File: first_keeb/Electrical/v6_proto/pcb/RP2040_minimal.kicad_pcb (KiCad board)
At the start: 2 copper layers, 77.7 x 77.5 mm, 71 parts, among them P1 USB-TYPE-C-016, Q1 SN74LV1T34DBV, SW1 SKRKAGE020, SW2 PTS647 SN70 SMTR2 LFS, SW3 PTS647 SN70 SMTR2 LFS, U1 NCP1117-3.3_SOT223, U2 LM4040DBZ-3, U3 PRTR5V0U2X, U4 W25Q32JVSS, U5 RP2040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

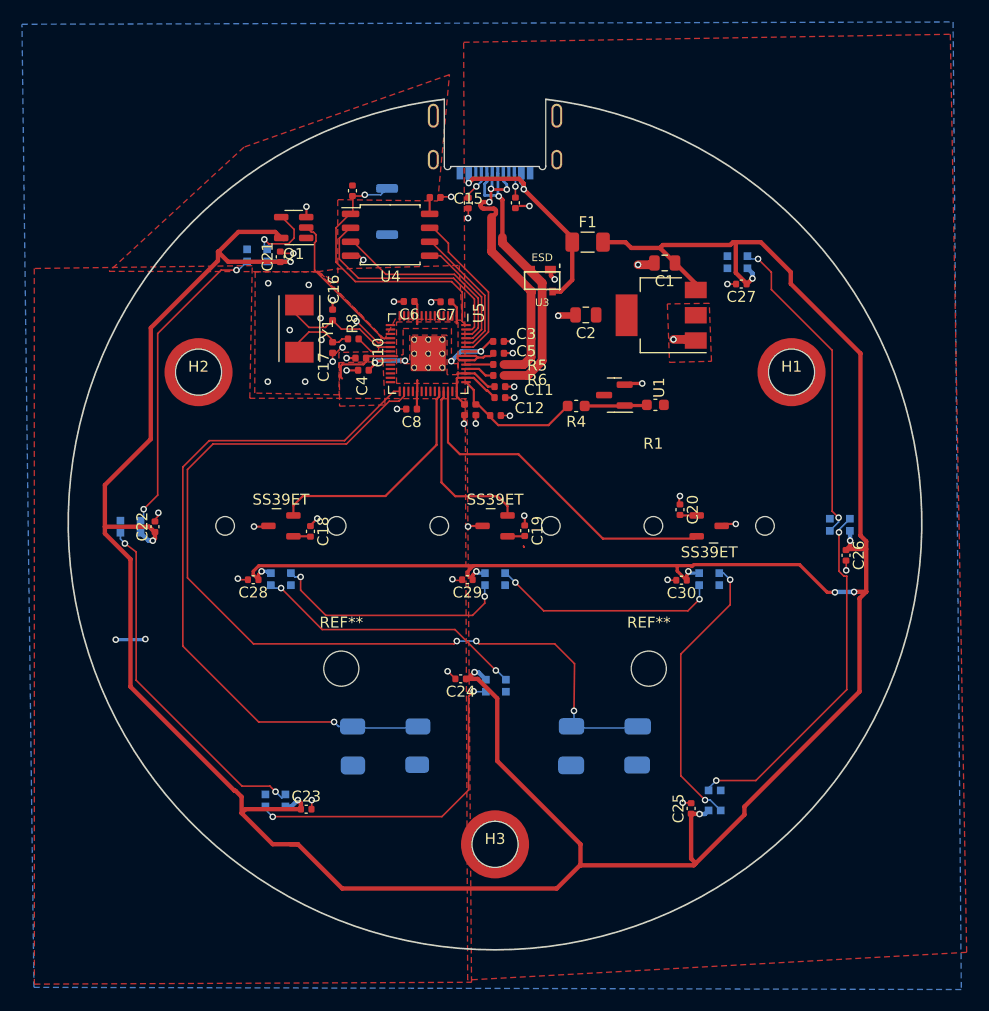
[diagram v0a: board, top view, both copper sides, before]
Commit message: make room for weights under pcb lower half
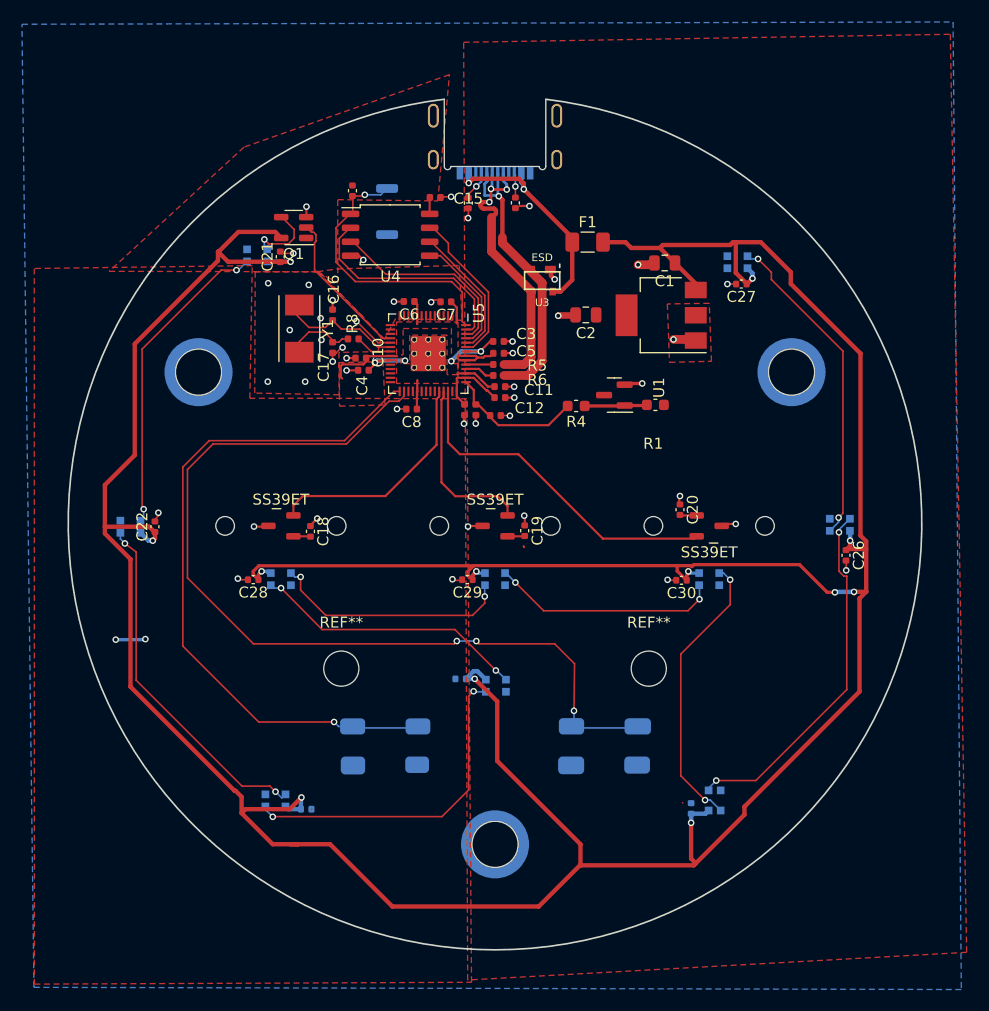
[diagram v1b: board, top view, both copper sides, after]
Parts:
- C23, C24, C25, H1, H2, H3: moved to B.Cu
- turned H1 to 180 degrees
- turned H2 to 180 degrees
- turned H3 to 180 degrees
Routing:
- net GND: track 43.6 -> 40.9 mm, vias 49 -> 46
- net +5V: track 333.0 -> 335.1 mm
